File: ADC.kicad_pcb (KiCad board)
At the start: 2 copper layers, 89.5 x 22 mm, 15 parts, among them J1 Conn_01x03, J2 Conn_02x06_Odd_Even, Q1 BC847, Q2 BC857, U1 SN74LVC1G175DCKT

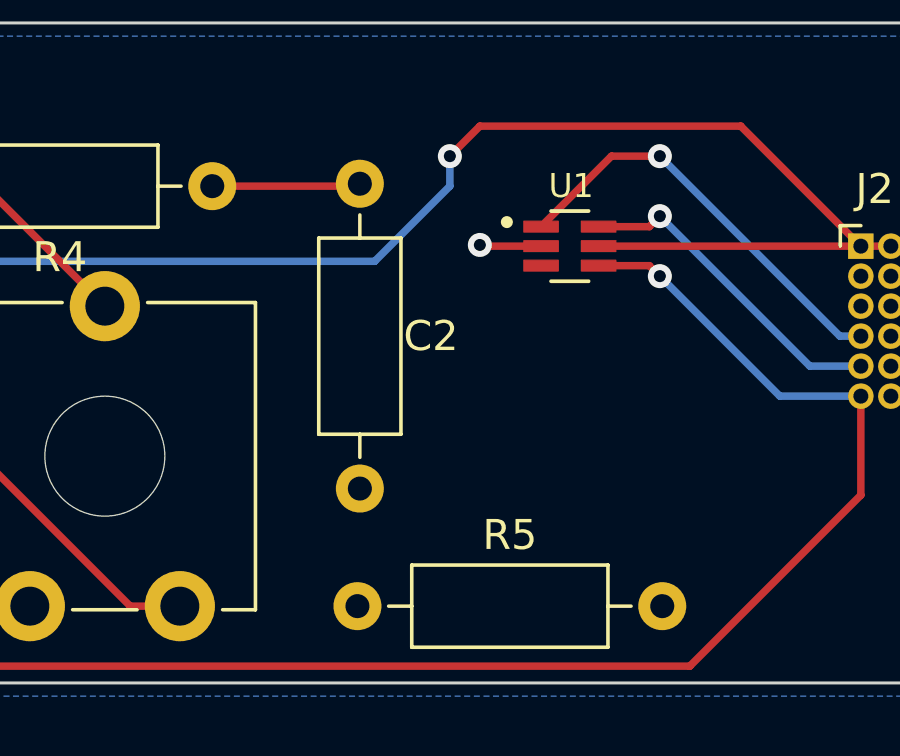
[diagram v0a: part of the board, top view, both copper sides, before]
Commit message: Fixed C2 connections
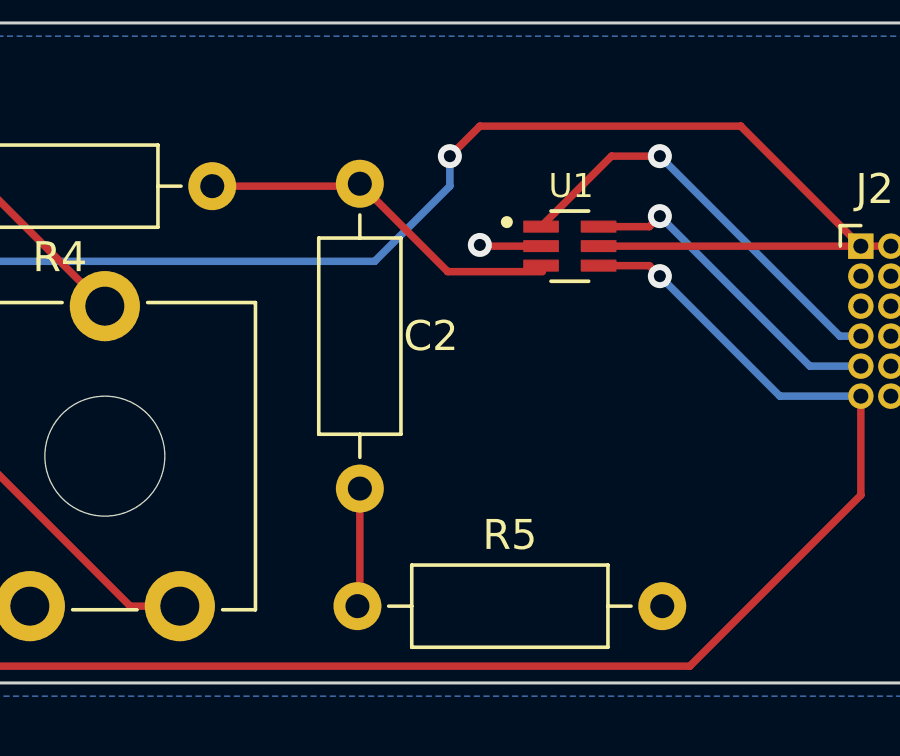
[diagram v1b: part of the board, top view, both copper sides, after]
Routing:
- net Net-(C2-Pad1): track 4.95 -> 12.3 mm
- net Net-(C2-Pad2): track 0.00 -> 3.95 mm
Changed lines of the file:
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@@
   (segment (start 164.04 79) (end 164 78.96) (width 0.25) (layer "F.Cu") (net 2))
   (via (at 164 78.96) (size 0.8) (drill 0.4) (layers "F.Cu" "B.Cu") (free) (net 2))
+  (segment (start 162.93 79.85) (end 166.09 79.85) (width 0.25) (layer "F.Cu") (net 3))
   (segment (start 155.08 77) (end 159.92 77) (width 0.25) (layer "F.Cu") (net 3))
+  (segment (start 160 76.92) (end 162.93 79.85) (width 0.25) (layer "F.Cu") (net 3))
   (segment (start 159.92 77) (end 160 76.92) (width 0.25) (layer "F.Cu") (net 3))
+  (segment (start 160 90.92) (end 159.92 91) (width 0.25) (layer "F.Cu") (net 4))
+  (segment (start 160 87.08) (end 160 90.92) (width 0.25) (layer "F.Cu") (net 4))
   (segment (start 99.84 77) (end 103.08 77) (width 0.25) (layer "F.Cu") (net 5))
   (segment (start 99.84 77) (end 92 77) (width 0.25) (layer "F.Cu") (net 5))
